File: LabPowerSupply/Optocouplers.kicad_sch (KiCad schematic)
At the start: 3 parts, among them U1 6N137, U1 74AHC04, U2 6N137

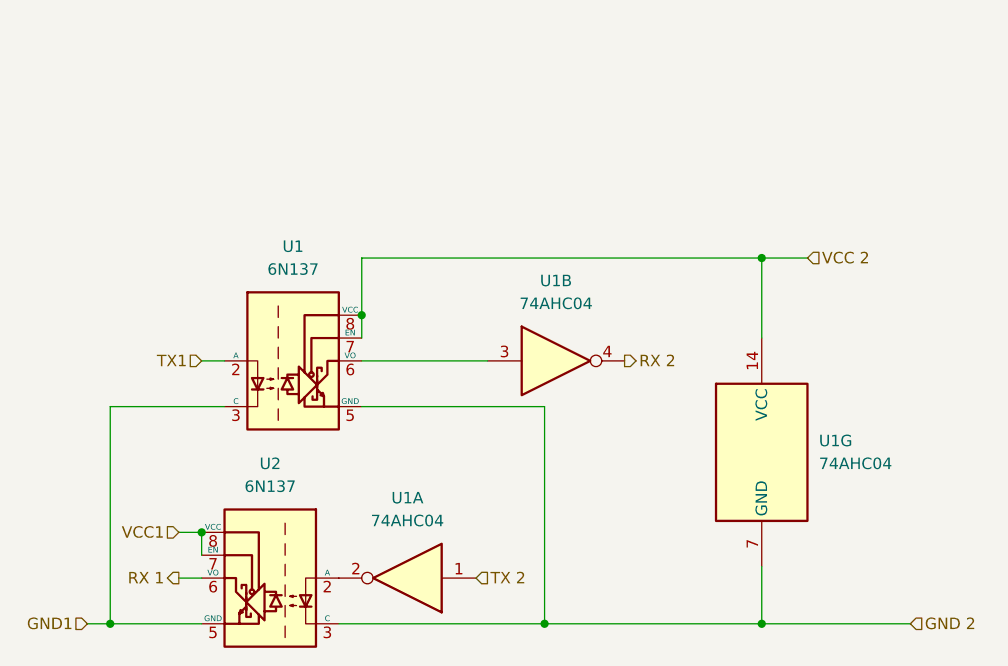
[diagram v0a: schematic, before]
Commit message: Finished first pass on the schematic
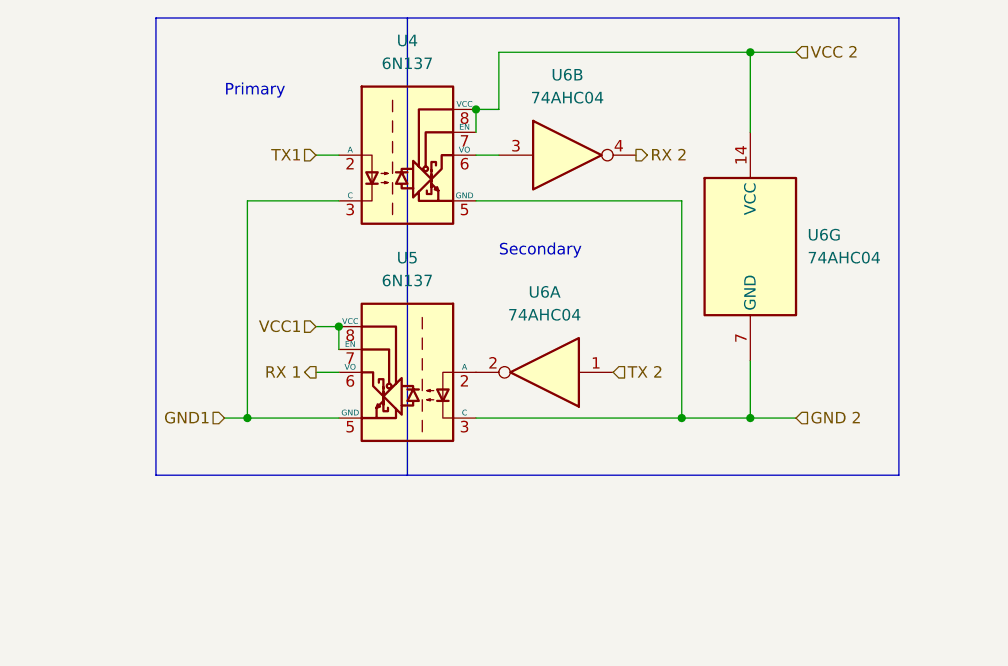
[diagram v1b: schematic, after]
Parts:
- renumbered U1 to U4, U2 to U5, U1 to U6
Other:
- note added: "Primary"
- note added: "Secondary"
- company: (none) -> George Mason University
- title: (none) -> Optocouplers
- moved on the sheet: U4, U5, U6A, U6B, U6G

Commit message: started PCB
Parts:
- removed U6: 74AHC04, Package_DIP:DIP-14_W7.62mm, symbol 74xx:74AHC04
- added U1: 74AHC04, Package_DIP:DIP-14_W7.62mm, symbol 74xx:74AHC04
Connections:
- net RX 2: now also U1.4
- net TX 2: now also U1.5
- net at U5.2 (A): now also U1.6
- net at U4.6 (VO): now also U1.3
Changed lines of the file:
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@@
     (comment 4 "The optocouplers allow for communication between the two")
-  )
-  (junction (at 162.56 111.76) (diameter 0) (color 0 0 0 0)
   )
   (junction (at 132.08 77.47) (diameter 0) (color 0 0 0 0)
@@
   (junction (at 106.68 111.76) (diameter 0) (color 0 0 0 0)
   )
-  (junction (at 162.56 71.12) (diameter 0) (color 0 0 0 0)
-  )
   (junction (at 116.84 101.6) (diameter 0) (color 0 0 0 0)
   )
@@
     (stroke (width 0) (type default) (color 0 0 0 0))
   )
-  (wire (pts (xy 154.94 111.76) (xy 162.56 111.76))
-    (stroke (width 0) (type default) (color 0 0 0 0))
-  )
-  (wire (pts (xy 162.56 111.76) (xy 167.64 111.76))
+  (wire (pts (xy 132.08 111.76) (xy 154.94 111.76))
     (stroke (width 0) (type default) (color 0 0 0 0))
   )
@@
     (stroke (width 0) (type default) (color 0 0 0 0))
   )
-  (wire (pts (xy 132.08 111.76) (xy 154.94 111.76))
-    (stroke (width 0) (type default) (color 0 0 0 0))
-  )
   (wire (pts (xy 132.08 82.55) (xy 134.62 82.55))
     (stroke (width 0) (type default) (color 0 0 0 0))
@@
     (stroke (width 0) (type default) (color 0 0 0 0))
   )
-  (wire (pts (xy 162.56 80.01) (xy 162.56 71.12))
-    (stroke (width 0) (type default) (color 0 0 0 0))
-  )
   (wire (pts (xy 114.3 106.68) (xy 116.84 106.68))
-    (stroke (width 0) (type default) (color 0 0 0 0))
-  )
-  (wire (pts (xy 162.56 105.41) (xy 162.56 111.76))
     (stroke (width 0) (type default) (color 0 0 0 0))
   )
@@
     (stroke (width 0) (type default) (color 0 0 0 0))
   )
-  (wire (pts (xy 162.56 71.12) (xy 167.64 71.12))
+  (wire (pts (xy 154.94 111.76) (xy 157.48 111.76))
     (stroke (width 0) (type default) (color 0 0 0 0))
   )
@@
     (stroke (width 0) (type default) (color 0 0 0 0))
   )
-  (wire (pts (xy 162.56 71.12) (xy 134.62 71.12))
+  (wire (pts (xy 134.62 71.12) (xy 157.48 71.12))
     (stroke (width 0) (type default) (color 0 0 0 0))
   )
@@
     (stroke (width 0) (type default) (color 0 0 0 0))
   )
-  (polyline (pts (xy 179.07 67.31) (xy 96.52 67.31))
+  (polyline (pts (xy 166.37 67.31) (xy 96.52 67.31))
     (stroke (width 0) (type default) (color 0 0 0 0))
   )
@@
     (stroke (width 0) (type default) (color 0 0 0 0))
   )
-  (polyline (pts (xy 124.46 118.11) (xy 179.07 118.11))
+  (polyline (pts (xy 124.46 118.11) (xy 166.37 118.11))
     (stroke (width 0) (type default) (color 0 0 0 0))
   )
-  (polyline (pts (xy 179.07 118.11) (xy 179.07 67.31))
+  (polyline (pts (xy 166.37 118.11) (xy 166.37 67.31))
     (stroke (width 0) (type default) (color 0 0 0 0))
   )
@@
     (effects (font (size 1.27 1.27)) (justify right))
   )
-  (hierarchical_label "GND 2" (shape input) (at 167.64 111.76 0)
+  (hierarchical_label "GND 2" (shape input) (at 157.48 111.76 0)
     (effects (font (size 1.27 1.27)) (justify left))
   )
-  (hierarchical_label "VCC 2" (shape input) (at 167.64 71.12 0)
+  (hierarchical_label "VCC 2" (shape input) (at 157.48 71.12 0)
     (effects (font (size 1.27 1.27)) (justify left))
   )
@@
     (effects (font (size 1.27 1.27)) (justify left))
   )
-  (symbol (lib_id "74xx:74AHC04") (at 139.7 106.68 180) (unit 1)
+  (symbol (lib_id "74xx:74AHC04") (at 142.24 82.55 0) (unit 2)
     (in_bom yes) (on_board yes) (fields_autoplaced)
-    (property "Reference" "U6" (id 0) (at 139.7 97.79 0))
-    (property "Value" "74AHC04" (id 1) (at 139.7 100.33 0))
-    (property "Footprint" "Package_DIP:DIP-14_W7.62mm" (id 2) (at 139.7 106.68 0)
+    (property "Reference" "U1" (id 0) (at 142.24 73.66 0))
+    (property "Value" "74AHC04" (id 1) (at 142.24 76.2 0))
+    (property "Footprint" "Package_DIP:DIP-14_W7.62mm" (id 2) (at 142.24 82.55 0)
       (effects (font (size 1.27 1.27)) hide)
     )
-    (property "Datasheet" "https://assets.nexperia.com/documents/data-sheet/74AHC_AHCT04.pdf" (id 3) (at 139.7 106.68 0)
+    (property "Datasheet" "https://assets.nexperia.com/documents/data-sheet/74AHC_AHCT04.pdf" (id 3) (at 142.24 82.55 0)
       (effects (font (size 1.27 1.27)) hide)
     )
@@
     (pin "7")
   )
-  (symbol (lib_id "74xx:74AHC04") (at 162.56 92.71 0) (unit 7)
+  (symbol (lib_id "74xx:74AHC04") (at 139.7 106.68 180) (unit 3)
     (in_bom yes) (on_board yes) (fields_autoplaced)
-    (property "Reference" "U6" (id 0) (at 168.91 91.4399 0)
-      (effects (font (size 1.27 1.27)) (justify left))
-    )
-    (property "Value" "74AHC04" (id 1) (at 168.91 93.9799 0)
-      (effects (font (size 1.27 1.27)) (justify left))
-    )
-    (property "Footprint" "Package_DIP:DIP-14_W7.62mm" (id 2) (at 162.56 92.71 0)
+    (property "Reference" "U1" (id 0) (at 139.7 97.79 0))
+    (property "Value" "74AHC04" (id 1) (at 139.7 100.33 0))
+    (property "Footprint" "Package_DIP:DIP-14_W7.62mm" (id 2) (at 139.7 106.68 0)
       (effects (font (size 1.27 1.27)) hide)
     )
-    (property "Datasheet" "https://assets.nexperia.com/documents/data-sheet/74AHC_AHCT04.pdf" (id 3) (at 162.56 92.71 0)
+    (property "Datasheet" "https://assets.nexperia.com/documents/data-sheet/74AHC_AHCT04.pdf" (id 3) (at 139.7 106.68 0)
       (effects (font (size 1.27 1.27)) hide)
     )
@@
     (pin "8")
   )
-  (symbol (lib_id "74xx:74AHC04") (at 142.24 82.55 0) (unit 2)
-    (in_bom yes) (on_board yes)
-    (property "Reference" "U6" (id 0) (at 142.24 73.66 0))
-    (property "Value" "74AHC04" (id 1) (at 142.24 76.2 0))
-    (property "Footprint" "Package_DIP:DIP-14_W7.62mm" (id 2) (at 142.24 82.55 0)
-      (effects (font (size 1.27 1.27)) hide)
-    )
-    (property "Datasheet" "https://assets.nexperia.com/documents/data-sheet/74AHC_AHCT04.pdf" (id 3) (at 142.24 82.55 0)
-      (effects (font (size 1.27 1.27)) hide)
-    )
-    (pin "1")
-    (pin "2")
-    (pin "3")
-    (pin "4")
-    (pin "5")
-    (pin "6")
-    (pin "8")
-    (pin "9")
-    (pin "10")
-    (pin "11")
-    (pin "12")
-    (pin "13")
-    (pin "14")
-    (pin "7")
-  )
   (symbol (lib_id "Isolator:6N137") (at 124.46 82.55 0) (unit 1)

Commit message: more work
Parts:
- renumbered U1 to Inverter2, U4 to Optocoupler1, U5 to Optocoupler2
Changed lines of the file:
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@@
   (symbol (lib_id "74xx:74AHC04") (at 142.24 82.55 0) (unit 2)
     (in_bom yes) (on_board yes) (fields_autoplaced)
-    (property "Reference" "U1" (id 0) (at 142.24 73.66 0))
+    (property "Reference" "Inverter2" (id 0) (at 142.24 73.66 0))
     (property "Value" "74AHC04" (id 1) (at 142.24 76.2 0))
     (property "Footprint" "Package_DIP:DIP-14_W7.62mm" (id 2) (at 142.24 82.55 0)
@@
   (symbol (lib_id "74xx:74AHC04") (at 139.7 106.68 180) (unit 3)
     (in_bom yes) (on_board yes) (fields_autoplaced)
-    (property "Reference" "U1" (id 0) (at 139.7 97.79 0))
+    (property "Reference" "Inverter2" (id 0) (at 139.7 97.79 0))
     (property "Value" "74AHC04" (id 1) (at 139.7 100.33 0))
     (property "Footprint" "Package_DIP:DIP-14_W7.62mm" (id 2) (at 139.7 106.68 0)
@@
   (symbol (lib_id "Isolator:6N137") (at 124.46 106.68 0) (mirror y) (unit 1)
     (in_bom yes) (on_board yes) (fields_autoplaced)
-    (property "Reference" "U5" (id 0) (at 124.46 93.98 0))
+    (property "Reference" "Optocoupler2" (id 0) (at 124.46 93.98 0))
     (property "Value" "6N137" (id 1) (at 124.46 96.52 0))
     (property "Footprint" "Package_DIP:DIP-8_W7.62mm" (id 2) (at 124.46 119.38 0)
@@
   (symbol (lib_id "Isolator:6N137") (at 124.46 82.55 0) (unit 1)
     (in_bom yes) (on_board yes) (fields_autoplaced)
-    (property "Reference" "U4" (id 0) (at 124.46 69.85 0))
+    (property "Reference" "Optocoupler1" (id 0) (at 124.46 69.85 0))
     (property "Value" "6N137" (id 1) (at 124.46 72.39 0))
     (property "Footprint" "Package_DIP:DIP-8_W7.62mm" (id 2) (at 124.46 95.25 0)

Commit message: Resistor footprints changed to 0603
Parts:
- Inverter2: value 74AHC04 -> (none); footprint Package_DIP:DIP-14_W7.62mm -> (none)
- Optocoupler1, Optocoupler2: value 6N137 -> (none); footprint Package_DIP:DIP-8_W7.62mm -> (none)
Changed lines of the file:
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@@
     (in_bom yes) (on_board yes) (fields_autoplaced)
     (property "Reference" "Inverter2" (id 0) (at 142.24 73.66 0))
-    (property "Value" "74AHC04" (id 1) (at 142.24 76.2 0))
-    (property "Footprint" "Package_DIP:DIP-14_W7.62mm" (id 2) (at 142.24 82.55 0)
+    (property "Value" "" (id 1) (at 142.24 76.2 0))
+    (property "Footprint" "" (id 2) (at 142.24 82.55 0)
       (effects (font (size 1.27 1.27)) hide)
     )
@@
     (in_bom yes) (on_board yes) (fields_autoplaced)
     (property "Reference" "Inverter2" (id 0) (at 139.7 97.79 0))
-    (property "Value" "74AHC04" (id 1) (at 139.7 100.33 0))
-    (property "Footprint" "Package_DIP:DIP-14_W7.62mm" (id 2) (at 139.7 106.68 0)
+    (property "Value" "" (id 1) (at 139.7 100.33 0))
+    (property "Footprint" "" (id 2) (at 139.7 106.68 0)
       (effects (font (size 1.27 1.27)) hide)
     )
@@
     (in_bom yes) (on_board yes) (fields_autoplaced)
     (property "Reference" "Optocoupler2" (id 0) (at 124.46 93.98 0))
-    (property "Value" "6N137" (id 1) (at 124.46 96.52 0))
-    (property "Footprint" "Package_DIP:DIP-8_W7.62mm" (id 2) (at 124.46 119.38 0)
+    (property "Value" "" (id 1) (at 124.46 96.52 0))
+    (property "Footprint" "" (id 2) (at 124.46 119.38 0)
       (effects (font (size 1.27 1.27)) hide)
     )
@@
     (in_bom yes) (on_board yes) (fields_autoplaced)
     (property "Reference" "Optocoupler1" (id 0) (at 124.46 69.85 0))
-    (property "Value" "6N137" (id 1) (at 124.46 72.39 0))
-    (property "Footprint" "Package_DIP:DIP-8_W7.62mm" (id 2) (at 124.46 95.25 0)
+    (property "Value" "" (id 1) (at 124.46 72.39 0))
+    (property "Footprint" "" (id 2) (at 124.46 95.25 0)
       (effects (font (size 1.27 1.27)) hide)
     )

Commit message: Added mcu capacitors, split 5v inductors
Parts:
- Inverter2: value (none) -> 74AHC04; footprint (none) -> Package_DIP:DIP-14_W7.62mm
- Optocoupler1, Optocoupler2: value (none) -> 6N137; footprint (none) -> Package_DIP:DIP-8_W7.62mm
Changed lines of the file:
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@@
     (in_bom yes) (on_board yes) (fields_autoplaced)
     (property "Reference" "Inverter2" (id 0) (at 142.24 73.66 0))
-    (property "Value" "" (id 1) (at 142.24 76.2 0))
-    (property "Footprint" "" (id 2) (at 142.24 82.55 0)
+    (property "Value" "74AHC04" (id 1) (at 142.24 76.2 0))
+    (property "Footprint" "Package_DIP:DIP-14_W7.62mm" (id 2) (at 142.24 82.55 0)
       (effects (font (size 1.27 1.27)) hide)
     )
@@
     (in_bom yes) (on_board yes) (fields_autoplaced)
     (property "Reference" "Inverter2" (id 0) (at 139.7 97.79 0))
-    (property "Value" "" (id 1) (at 139.7 100.33 0))
-    (property "Footprint" "" (id 2) (at 139.7 106.68 0)
+    (property "Value" "74AHC04" (id 1) (at 139.7 100.33 0))
+    (property "Footprint" "Package_DIP:DIP-14_W7.62mm" (id 2) (at 139.7 106.68 0)
       (effects (font (size 1.27 1.27)) hide)
     )
@@
     (in_bom yes) (on_board yes) (fields_autoplaced)
     (property "Reference" "Optocoupler2" (id 0) (at 124.46 93.98 0))
-    (property "Value" "" (id 1) (at 124.46 96.52 0))
-    (property "Footprint" "" (id 2) (at 124.46 119.38 0)
+    (property "Value" "6N137" (id 1) (at 124.46 96.52 0))
+    (property "Footprint" "Package_DIP:DIP-8_W7.62mm" (id 2) (at 124.46 119.38 0)
       (effects (font (size 1.27 1.27)) hide)
     )
@@
     (in_bom yes) (on_board yes) (fields_autoplaced)
     (property "Reference" "Optocoupler1" (id 0) (at 124.46 69.85 0))
-    (property "Value" "" (id 1) (at 124.46 72.39 0))
-    (property "Footprint" "" (id 2) (at 124.46 95.25 0)
+    (property "Value" "6N137" (id 1) (at 124.46 72.39 0))
+    (property "Footprint" "Package_DIP:DIP-8_W7.62mm" (id 2) (at 124.46 95.25 0)
       (effects (font (size 1.27 1.27)) hide)
     )

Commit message: Changed most parts to smd
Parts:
- Optocoupler1, Optocoupler2: footprint Package_DIP:DIP-8_W7.62mm -> Package_DIP:PowerIntegrations_SMD-8
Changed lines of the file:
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@@
     (property "Reference" "Optocoupler2" (id 0) (at 124.46 93.98 0))
     (property "Value" "6N137" (id 1) (at 124.46 96.52 0))
-    (property "Footprint" "Package_DIP:DIP-8_W7.62mm" (id 2) (at 124.46 119.38 0)
+    (property "Footprint" "Package_DIP:PowerIntegrations_SMD-8" (id 2) (at 124.46 119.38 0)
       (effects (font (size 1.27 1.27)) hide)
     )
@@
     (property "Reference" "Optocoupler1" (id 0) (at 124.46 69.85 0))
     (property "Value" "6N137" (id 1) (at 124.46 72.39 0))
-    (property "Footprint" "Package_DIP:DIP-8_W7.62mm" (id 2) (at 124.46 95.25 0)
+    (property "Footprint" "Package_DIP:PowerIntegrations_SMD-8" (id 2) (at 124.46 95.25 0)
       (effects (font (size 1.27 1.27)) hide)
     )

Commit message: routing is weird
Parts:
- Inverter2: footprint Package_DIP:DIP-14_W7.62mm -> Package_SO:SSOP-14_5.3x6.2mm_P0.65mm
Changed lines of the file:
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@@
     (property "Reference" "Inverter2" (id 0) (at 142.24 73.66 0))
     (property "Value" "74AHC04" (id 1) (at 142.24 76.2 0))
-    (property "Footprint" "Package_DIP:DIP-14_W7.62mm" (id 2) (at 142.24 82.55 0)
+    (property "Footprint" "Package_SO:SSOP-14_5.3x6.2mm_P0.65mm" (id 2) (at 142.24 82.55 0)
       (effects (font (size 1.27 1.27)) hide)
     )
@@
     (property "Reference" "Inverter2" (id 0) (at 139.7 97.79 0))
     (property "Value" "74AHC04" (id 1) (at 139.7 100.33 0))
-    (property "Footprint" "Package_DIP:DIP-14_W7.62mm" (id 2) (at 139.7 106.68 0)
+    (property "Footprint" "Package_SO:SSOP-14_5.3x6.2mm_P0.65mm" (id 2) (at 139.7 106.68 0)
       (effects (font (size 1.27 1.27)) hide)
     )
